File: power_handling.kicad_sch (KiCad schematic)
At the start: 57 parts, among them J2 usb_c, SW1 CHS-01TA, U1 TPS62130, U12 FSUSB42MUX, U13 AP22802AW5-7, U2 MIC5365-1.8YC5-TR, U3 TPS62130, U4 MIC5365-0.9YC5-TR

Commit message: production preparation
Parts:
- R44, R7: value 49.9 -> 49.9R
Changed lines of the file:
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@@
 			)
 		)
-		(property "Value" "49.9"
+		(property "Value" "49.9R"
 			(at 243.84 39.624 0)
 			(effects
@@
 			)
 		)
-		(property "Value" "49.9"
+		(property "Value" "49.9R"
 			(at 135.89 39.624 0)
 			(effects

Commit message: final touches
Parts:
- D11, D12, D9: value PESD0402-050 -> PESD0402V05; Function MIC -> USB
- SW1: value CHS-01TA -> SMXS‑01K‑TP; Availability In Stock -> (none); Check_prices https://www.snapeda.com/parts/CHS-01TA/Nidec/view-part/?ref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 -> (none); MF Nidec Copal -> SM Switch; MP CHS-01TA -> SMXS‑01K‑TP; Package None -> (none); Price None -> (none); SnapEDA_Link https://www.snapeda.com/parts/CHS-01TA/Nidec/view-part/?ref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 -> (none)
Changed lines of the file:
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@@
 			)
 		)
-		(property "Value" "PESD0402-050"
+		(property "Value" "PESD0402V05"
 			(at 133.858 102.108 0)
 			(effects
@@
 			)
 		)
-		(property "Description" "PESD0402-050, 5V TVS, 0.3pF"
+		(property "Description" "PESD0402V05, 5V TVS, 0.3pF"
 			(at 129.54 109.22 0)
 			(effects
@@
 			)
 		)
-		(property "Function" "MIC"
+		(property "Function" "USB"
 			(at 129.54 109.22 90)
 			(effects
@@
 			)
 		)
-		(property "Value" "PESD0402-050"
+		(property "Value" "PESD0402V05"
 			(at 126.238 102.108 0)
 			(effects
@@
 			)
 		)
-		(property "Description" "PESD0402-050, 5V TVS, 0.3pF"
+		(property "Description" "PESD0402V05, 5V TVS, 0.3pF"
 			(at 121.92 109.22 0)
 			(effects
@@
 			)
 		)
-		(property "Function" "MIC"
+		(property "Function" "USB"
 			(at 121.92 109.22 90)
 			(effects
@@
 			)
 		)
-		(property "Description" ""
+		(property "Description" "2345986-1"
 			(at 78.74 100.33 0)
 			(effects
@@
 			)
 		)
-		(property "Value" "CHS-01TA"
+		(property "Value" "SMXS‑01K‑TP"
 			(at 25.4 173.736 0)
 			(effects
@@
 			)
 		)
-		(property "MF" "Nidec Copal"
+		(property "MF" "SM Switch"
 			(at 20.32 176.53 0)
 			(effects
@@
 			)
 		)
-		(property "Package" "None"
-			(at 20.32 176.53 0)
-			(effects
-				(font
-					(size 1.27 1.27)
-				)
-				(justify bottom)
-				(hide yes)
-			)
-		)
-		(property "Price" "None"
-			(at 20.32 176.53 0)
-			(effects
-				(font
-					(size 1.27 1.27)
-				)
-				(justify bottom)
-				(hide yes)
-			)
-		)
-		(property "SnapEDA_Link" "https://www.snapeda.com/parts/CHS-01TA/Nidec/view-part/?ref=snap"
-			(at 20.32 176.53 0)
-			(effects
-				(font
-					(size 1.27 1.27)
-				)
-				(justify bottom)
-				(hide yes)
-			)
-		)
-		(property "MP" "CHS-01TA"
-			(at 20.32 176.53 0)
-			(effects
-				(font
-					(size 1.27 1.27)
-				)
-				(justify bottom)
-				(hide yes)
-			)
-		)
-		(property "Availability" "In Stock"
-			(at 20.32 176.53 0)
-			(effects
-				(font
-					(size 1.27 1.27)
-				)
-				(justify bottom)
-				(hide yes)
-			)
-		)
-		(property "Check_prices" "https://www.snapeda.com/parts/CHS-01TA/Nidec/view-part/?ref=eda"
+		(property "MP" "SMXS‑01K‑TP"
 			(at 20.32 176.53 0)
 			(effects
@@
 			)
 		)
-		(property "Value" "PESD0402-050"
+		(property "Value" "PESD0402V05"
 			(at 33.528 188.722 90)
 			(effects
@@
 			)
 		)
-		(property "Description" "PESD0402-050, 5V TVS, 0.3pF"
+		(property "Description" "PESD0402V05, 5V TVS, 0.3pF"
 			(at 39.37 181.61 0)
 			(effects
@@
 			)
 		)
-		(property "Function" "MIC"
+		(property "Function" "USB"
 			(at 39.37 181.61 90)
 			(effects

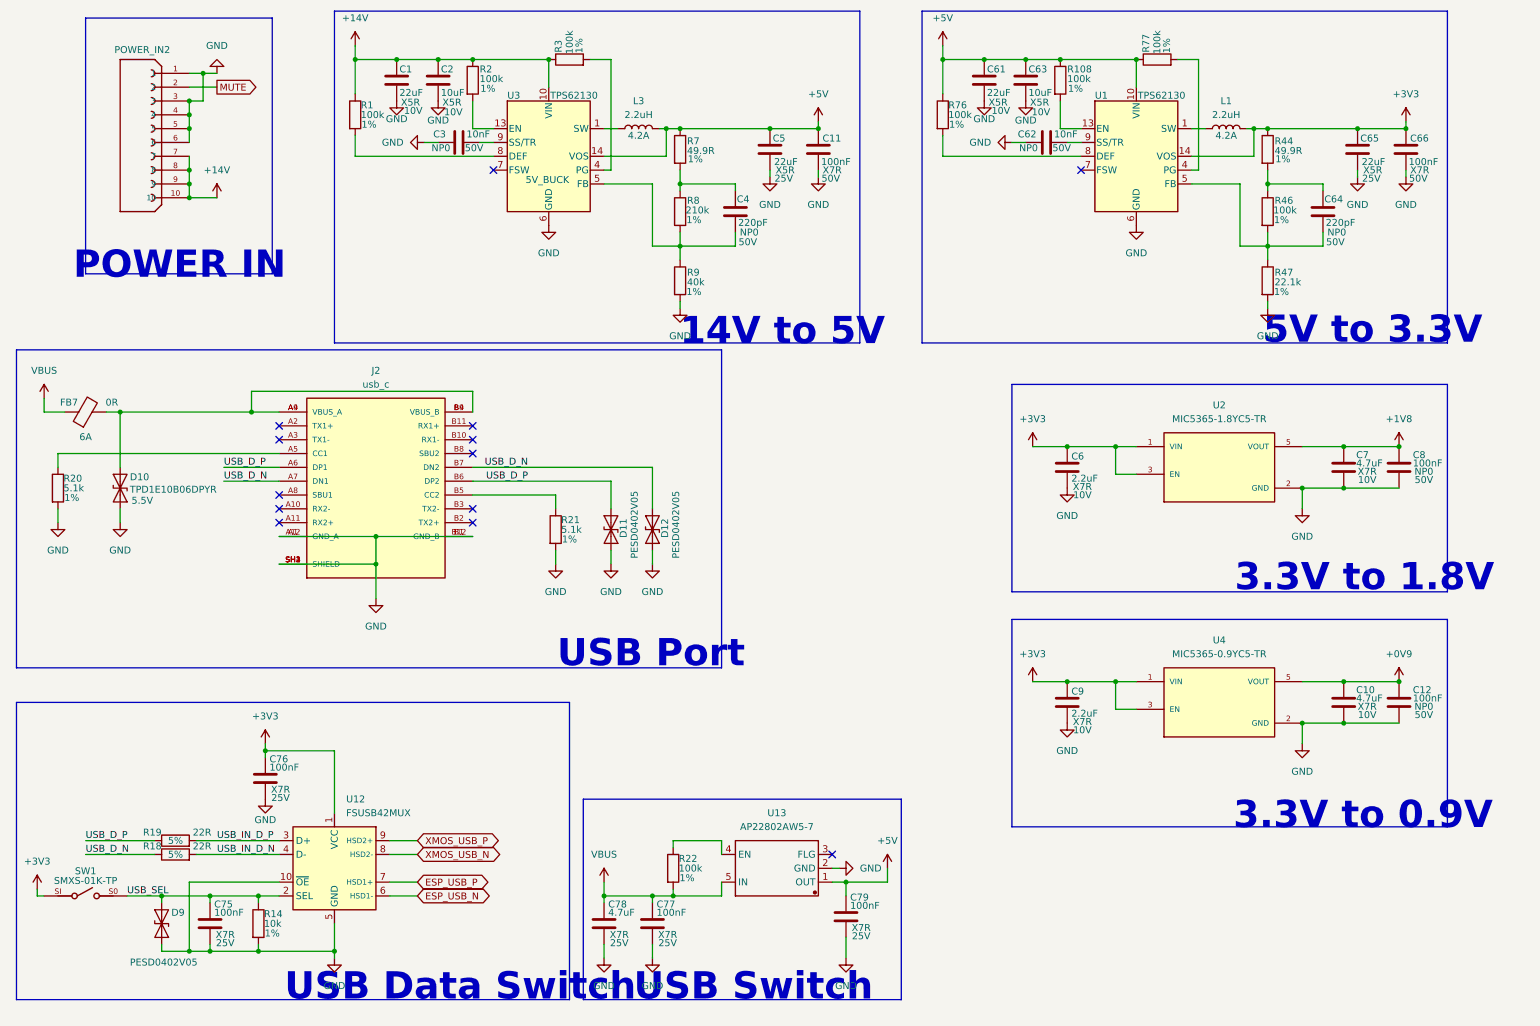
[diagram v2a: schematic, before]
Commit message: modifications for manufacturing
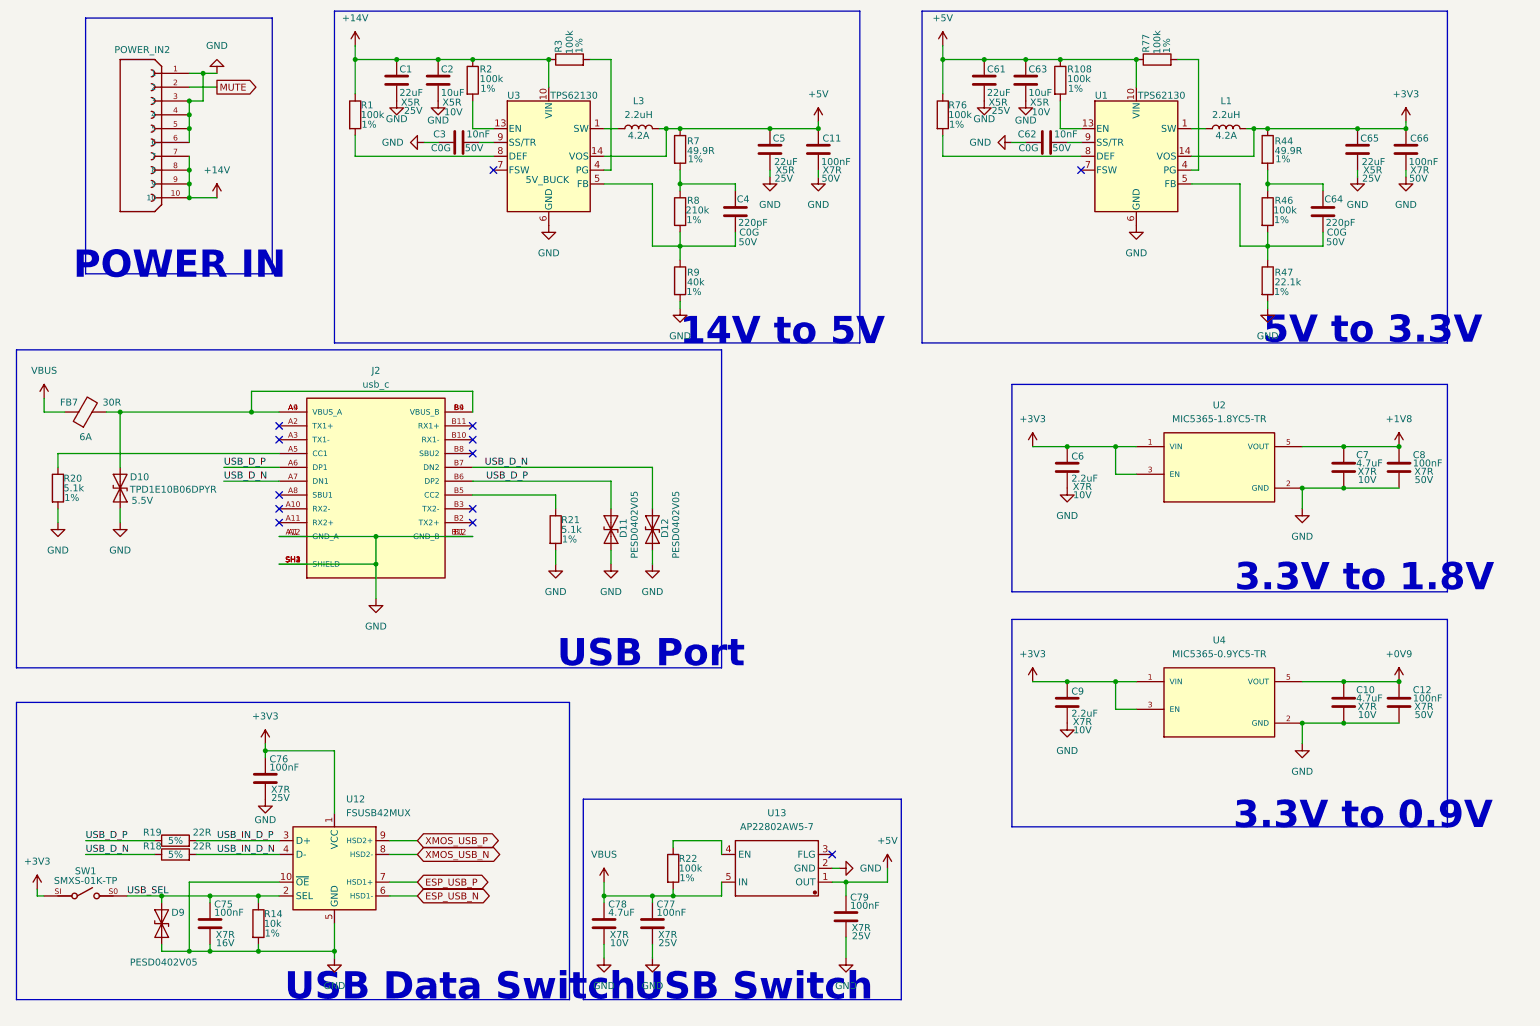
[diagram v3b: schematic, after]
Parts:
- C1, C61: Supplier Part (none) -> C45783; Voltage 10V -> 25V
- C10, C7: Supplier Part (none) -> C913474
- C11, C66: Supplier Part (none) -> C49678
- C12, C8: footprint Capacitor_SMD:C_0603_1608Metric -> Capacitor_SMD:C_0805_2012Metric; Dielectric NP0 -> X7R
- C2, C63: Supplier Part (none) -> C15850
- C3, C62: Dielectric NP0 -> C0G; Supplier Part (none) -> C15195
- C4, C64: Dielectric NP0 -> C0G; Supplier Part (none) -> C156398
- C5, C65: Supplier Part (none) -> C45783
- C6, C9: Supplier Part (none) -> C86018
- C75: Supplier Part (none) -> C1525; Voltage 25V -> 16V
- C76, C77, C79: Supplier Part (none) -> C14663
- C78: Supplier Part (none) -> C913474; Voltage 25V -> 10V
- D10: MANUFACTURER (none) -> Texas Instruments; MP (none) -> TPD1E10B06DPYR; Supplier Part (none) -> C48260
- D11, D9: MANUFACTURER (none) -> DOWO; MP (none) -> PESD0402V05; Manufacturer (none) -> DOWO; Part (none) -> C19626254; Supplier Part (none) -> C19626254
- D12: MANUFACTURER (none) -> DOWO; MP (none) -> PESD0402V05; Supplier Part (none) -> C19626254
- FB7: value 0R -> 30R; MANUFACTURER (none) -> Murata Electronics; MP (none) -> BLM18PG300SN1D; Supplier Part (none) -> C17305
- J2: footprint Onju:usb_c -> Onju:USB-C-SMD_TYPE-C-USB-18; Availability In Stock -> (none); Check_prices https://www.snapeda.com/parts/2345986-1/TE+Connectivity/vie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 -> (none); Description_1 USB TYPE C 3.1 TOP MOUNT DUAL SMT 1.63CH -> (none); MANUFACTURER TE Connectivity -> MOLEX; MAXIMUM_PACKAGE_HEIGHT 3.16mm -> (none); MF TE Connectivity -> (none); MP 2345986-1 -> 1054500101; PARTREV C -> (none); Package None -> SMD; Price None -> (none); STANDARD Manufacturer Recommendations -> (none); SnapEDA_Link https://www.snapeda.com/parts/2345986-1/TE+Connectivity/vie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 -> (none); Supplier Part (none) -> C134092
- L1, L3: MANUFACTURER (none) -> Sunlord; MP (none) -> SDFL1005P2R2KTF; Supplier Part (none) -> C49067
- POWER_IN2: Availability In Stock -> (none); Check_prices https://www.snapeda.com/parts/FH34SRJ-10S-0.5SH(50)/Hirose/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 -> (none); MF Hirose Electric -> (none); PARTREV Apr.1.2022 -> (none); Package None -> SMD,P=0.5mm,Surface Mount，Right Angle; Price None -> (none); STANDARD Manufacturer Recommendations -> (none); Supplier Part (none) -> C324723
- R1, R108, R2, R22, R3, R76, R77: Supplier Part (none) -> C25530
- R14: Supplier Part (none) -> C25744
- R18, R19: Supplier Part (none) -> C25092
- R20, R21: Supplier Part (none) -> C25905
- R44, R7: Supplier Part (none) -> C23185
- R46: Supplier Part (none) -> C25803
- R47: Supplier Part (none) -> C25961
- R8: Supplier Part (none) -> C22952
- R9: Supplier Part (none) -> C3016445
- SW1: MANUFACTURER (none) -> SM Switch; Supplier Part (none) -> C5439760
- U1, U3: MANUFACTURER (none) -> Texas Instruments; MP (none) -> TPS62130ARGTR; Supplier Part (none) -> C337502
- U12: Function (none) -> USB; MANUFACTURER (none) -> onsemi; MP (none) -> FSUSB42MUX; Supplier Part (none) -> C11355
- U13: MANUFACTURER (none) -> Diodes Incorporated; MP (none) -> AP22802AW5-7
- U2: MANUFACTURER Micrel -> Microchip Tech; Supplier Part (none) -> C626087

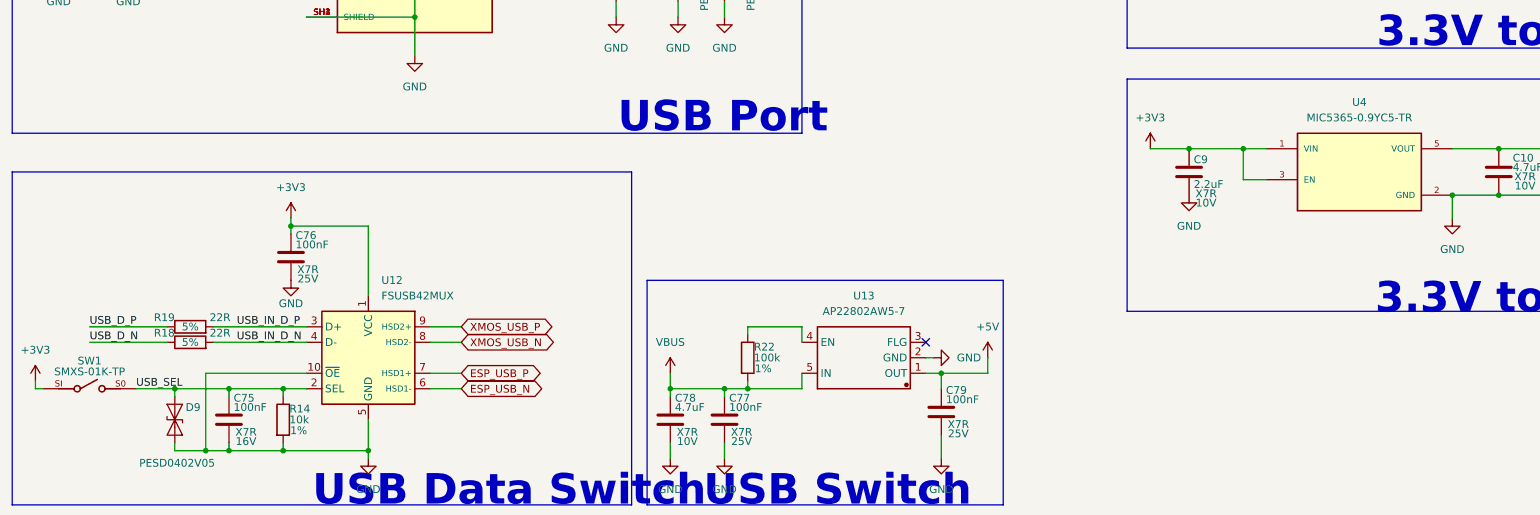
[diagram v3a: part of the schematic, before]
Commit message: modifications for manufacturing
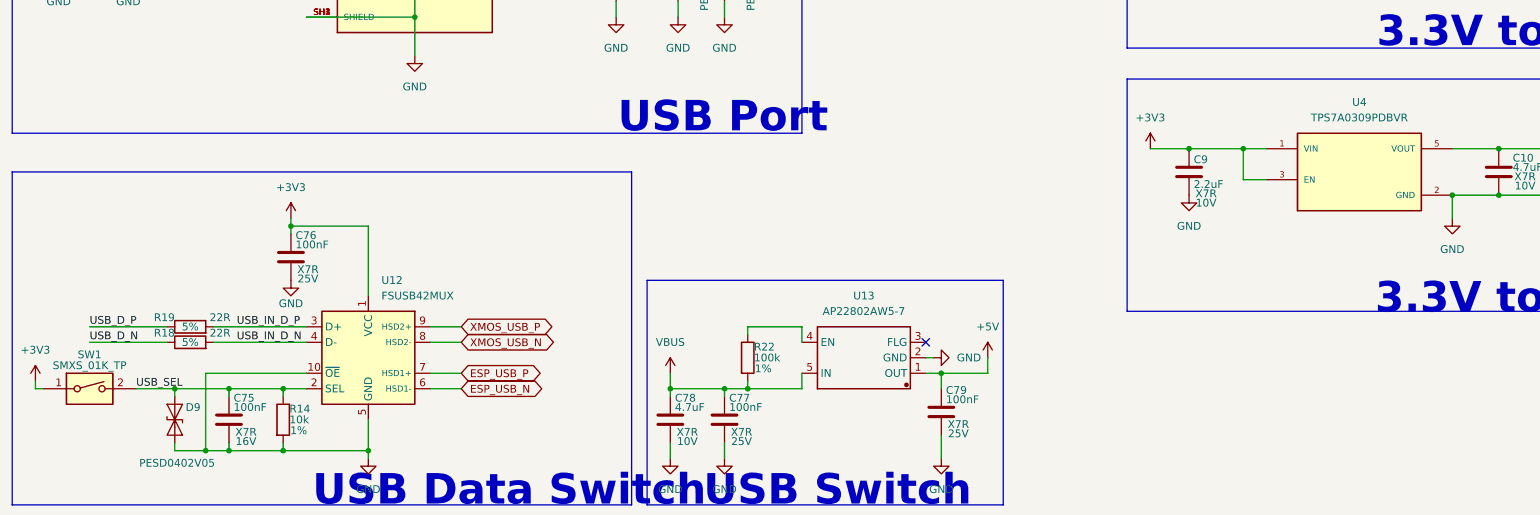
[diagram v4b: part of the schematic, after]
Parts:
- removed SW1: SMXS‑01K‑TP, Onju:CHS-01TA, symbol New_Library:CHS-01TA
- added SW1: SMXS_01K_TP, Onju:SW-SMD_2P-L6.2-W2.5-LS9.4, symbol Switch:SW_DIP_x01
- C12, C8: Supplier Part (none) -> C49678
- D10: Manufacturer (none) -> Texas Instruments; Manufacturer Part (none) -> TPD1E10B06DPYR
- D11, D9: Manufacturer Part (none) -> PESD0402V05
- D12: Manufacturer (none) -> DOWO; Manufacturer Part (none) -> PESD0402V05
- FB7: Manufacturer Part (none) -> BLM18PG300SN1D
- J2: Manufacturer (none) -> MOLEX; Manufacturer Part (none) -> 1054500101
- L1, L3: MANUFACTURER Sunlord -> BOURNS; MP SDFL1005P2R2KTF -> SRP4020TA-2R2M; Manufacturer (none) -> BOURNS; Manufacturer Part (none) -> SRP4020TA-2R2M; Supplier Part C49067 -> C719179
- POWER_IN2: Manufacturer (none) -> Hirose; Manufacturer Part (none) -> FH34SRJ-10S-0.5SH(50)
- U1, U3: Manufacturer (none) -> Texas Instruments; Manufacturer Part (none) -> TPS62130ARGTR
- U12: Manufacturer (none) -> onsemi; Manufacturer Part (none) -> FSUSB42MUX
- U2: Manufacturer (none) -> Microchip Tech; Manufacturer Part (none) -> MIC5365-1.8YC5-TR
- U4: value MIC5365-0.9YC5-TR -> TPS7A0309PDBVR; footprint Onju:SOT65P210X110-5N -> Package_TO_SOT_SMD:SOT-23-5; MANUFACTURER Micrel -> Texas Instruments; MP MIC5365-0.9YC5-TR -> TPS7A0309PDBVR; Manufacturer (none) -> Texas Instruments; Manufacturer Part (none) -> TPS7A0309PDBVR; Supplier Part (none) -> C2977167
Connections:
- net +3V3: now also SW1.1
- net USB_SEL: now also SW1.2
